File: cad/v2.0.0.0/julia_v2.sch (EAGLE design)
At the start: 32 parts, among them J1 NHD-5.0-800480TF-ATXL-CTP_LCD, J2 NHD-5.0-800480TF-ATXL-CTP_TOU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, U1 RMLV0416EGSB-4S2HA1, U2 EP2C5T144I8, U3 FAN5333BSX, U4 NCP565ST12T3G, U5 LP3965EMP-3.3/NOPB, U6 LP3965EMP-3.3/NOPB

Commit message: v2 update, power and config chip
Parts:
- added C14: 0.1uF, microbuilder:CAP_CERAMIC0805
- added C15: 4.7uF, ik:CPOL
- added FB1: 600R/1A, microbuilder:FERRITE
- added J3: ISP Header (AS), fab:CONN_05X2SHD
- added J4: JTAG Header, fab:CONN_05X2SHD
- added LED1, LED3: RED, led:LEDCHIPLED_0805
- added LED2: GREEN, led:LEDCHIPLED_0805
- added OSC1: (no value), ik:ASV-50.000MHZ-EJ-T
- added R10, R11, R12, R13, R8, R9: 10k, microbuilder:RESISTOR0805
- added R14, R15, R16: 1k, microbuilder:RESISTOR0805
- added R2, R3, R5: 47, microbuilder:RESISTOR0805
- added R4, R6, R7: 27, microbuilder:RESISTOR0805
- added SJ1: (no value), jumper:SJ2WW
- added TP6: TPB1,27, testpad:TPB1,27
- added U$31: EPCQ4ASI8N, ik:EPCQ4ASI8N
- R1: device microbuilder:RESISTOR_0805MP -> microbuilder:RESISTOR0805
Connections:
- new net ADSO: U$31.DATA0
- new net ASDO: J3.9, U2B.IO_3
- new net CE_N: J3.6, R9.2, U2A.!CE
- new net CONFIG_N: J3.5, R10.1, U2A.!CONFIG
- new net CONF_DONE: J3.3, LED2.C, R12.1, U2A.CONF_DONE
- new net CSO_N: J3.8, U$31.CS_N, U2B.IO_2
- new net DATA0: J3.7, R8.1, U$31.DATA1, U2A.DATA0
- new net DCLK: J3.1, R6.1, U$31.DCLK
- new net GCLK: R4.1, TP6.TP, U2A.CLK7
- new net JTAG_TCK: J4.1, R7.2
- new net JTAG_TDI: J4.9, R16.1, U2B.TDI
- new net JTAG_TDO: J4.3, U2B.TDO
- new net JTAG_TMS: J4.5, R15.1, U2B.TMS
- new net N$10: R14.2, R7.1, U2B.TCK
- new net N$11: C2.P$1, L1.2, SJ1.2, U3.VIN
- new net N$2: LED1.A, R2.2
- new net N$3: C14.P$1, C15.+, FB1.P$2, OSC1.EN, OSC1.VDD
- new net N$5: OSC1.OUT, R4.2
- new net N$6: LED3.A, R5.2
- new net N$7: R13.1, R6.2, U2A.DCLK
- new net N$9: LED2.A, R3.2
- new net STATUS_N: R11.1, U2A.!STATUS
- net 3V3IO: now also FB1.P$1, J3.4, J4.4, LED3.C, R10.2, R11.2, R12.2, R13.2, R15.2, R16.2, R8.2, U$31.VCC@1, U$31.VCC@2, U$31.VCC@3
- net GND: now also C14.P$2, C15.-, J3.10, J3.2, J4.10, J4.2, OSC1.GND, R14.1, R2.1, R3.1, R5.1, R9.1, U$31.GND, U2A.CLK0, U2A.CLK1, U2A.CLK2, U2A.CLK3, U2A.CLK4, U2A.CLK5, U2A.CLK6, U2B.MSEL0, U2B.MSEL1
- net VCC3V3: now also LED1.C, SJ1.3; no longer C2.P$1, L1.2, U3.VIN
- net VIN: now also F1.2, SJ1.1
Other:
- note added: "MSEL0/1 0,0 for AS (20MHz)"
- moved on the sheet: U2A, U2B, U2C

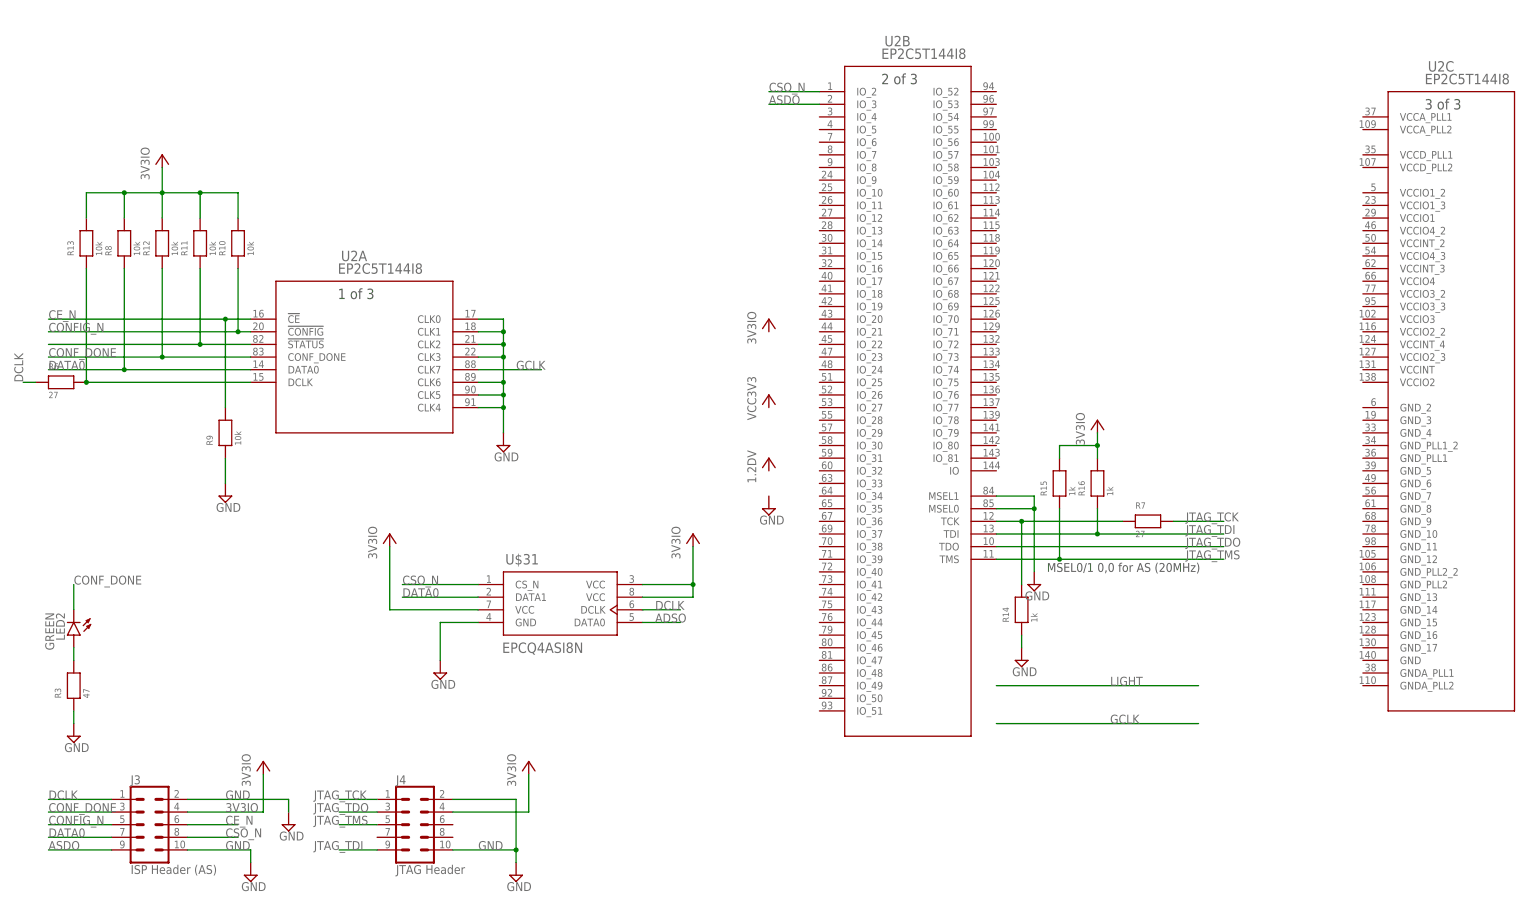
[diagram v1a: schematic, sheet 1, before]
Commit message: Julia v2.0.0.0 schematic and BOM
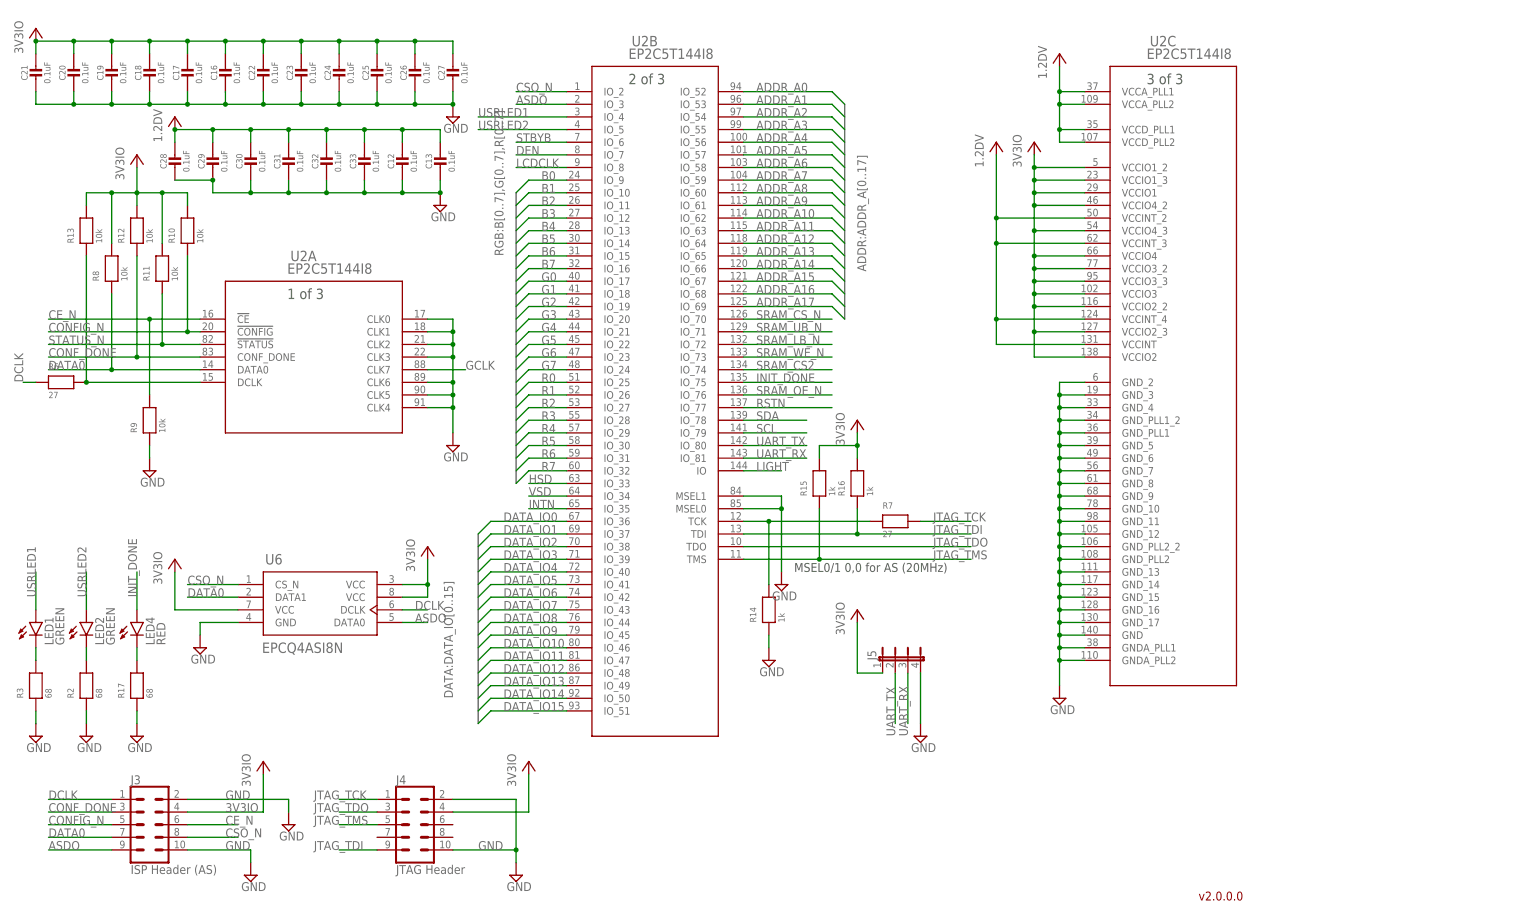
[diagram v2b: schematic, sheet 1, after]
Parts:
- removed TP3: TPB1,27, testpad:TPB1,27
- removed U$31: EPCQ4ASI8N, ik:EPCQ4ASI8N
- added C16, C17, C18, C19, C20, C21, C22, C23, C24, C25, C26, C27, C28, C29, C30, C31, C32, C33: 0.1uF, microbuilder:CAP_CERAMIC0805
- added J5: (no value), jumper:JP4E
- added LED4: RED, led:LEDCHIPLED_0805
- added R17: 68, microbuilder:RESISTOR0805
- added TP7: TPB1,27, testpad:TPB1,27
- C12: value 68uF -> 0.1uF; device microbuilder:CAP_CERAMIC1206 -> microbuilder:CAP_CERAMIC0805; DPN 445-14673-1-ND -> 478-12799-1-ND; MPN C3216X5R1A686M160AC -> 0805ZD104KAT2A
- C13: value 33uF -> 0.1uF; device ik:CPOL -> microbuilder:CAP_CERAMIC0805; DPN 478-5350-1-ND -> 478-12799-1-ND; MPN TLJP336M010R3500 -> 0805ZD104KAT2A
- F1: value (none) -> 3.5A
- LED1: value RED -> GREEN; DPN 67-1552-1-ND -> 67-1553-1-ND; MPN SML-LXT0805IW-TR -> ML-LXT0805IW-TR
- OSC1: value (none) -> 50MHz
- R10, R11, R12, R13, R8, R9: DPN (none) -> 311-10.0KCRCT-ND; MPN (none) -> RC0805FR-0710KL
- R14, R15, R16: DPN (none) -> 311-1.00KCRCT-ND; MPN (none) -> RC0805FR-071KL
- R2, R3: value 47 -> 68; DPN (none) -> 311-68.0CRCT-ND; MPN (none) -> RC0805FR-0768RL
- R4: value 27 -> 68; DPN (none) -> 311-68.0CRCT-ND; MPN (none) -> RC0805FR-0768RL
- R5: value 47 -> 27; DPN (none) -> 311-27ARCT-ND; MPN (none) -> RC0805JR-0727RL
- R6, R7: DPN (none) -> 311-27ARCT-ND; MPN (none) -> RC0805JR-0727RL
- U2: DPN (none) -> 544-2138-ND; MPN (none) -> EP2C5T144I8
- U6: value LP3965EMP-3.3/NOPB -> EPCQ4ASI8N; device ik:LP3965EMP-3.3/NOPB -> ik:EPCQ4ASI8N
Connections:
- removed net ADSO: U$31.DATA0
- removed net CLKIN: J1.CLKIN
- removed net N$2: LED1.A, R2.2
- removed net N$4: C5.P$1
- removed net VCC3V3: C13.+, LED1.C, SJ1.3, TP3.TP, U6.SENSE, U6.VOUT
- new net INIT_DONE: LED4.A, U2B.IO_75
- new net LCDCLK: J1.CLKIN, U2B.IO_8
- new net N$12: LED4.C, R17.2
- new net N$13: LED2.C, R2.2
- new net UART_RX: J5.3, U2B.IO_81
- new net UART_TX: J5.2, U2B.IO_80
- new net USRLED1: LED1.A, U2B.IO_4
- new net USRLED2: LED2.A, U2B.IO_5
- net 1.2DV: now also C12.P$1, C13.P$1, C28.P$1, C29.P$1, C30.P$1, C31.P$1, C32.P$1, C33.P$1, U2C.VCCA_PLL1, U2C.VCCA_PLL2, U2C.VCCD_PLL1, U2C.VCCD_PLL2, U2C.VCCINT, U2C.VCCINT_2, U2C.VCCINT_3, U2C.VCCINT_4
- net 3V3IO: now also C16.P$1, C17.P$1, C18.P$1, C19.P$1, C20.P$1, C21.P$1, C22.P$1, C23.P$1, C24.P$1, C25.P$1, C26.P$1, C27.P$1, C5.P$1, J5.1, LED3.A, SJ1.3, U2C.VCCIO1, U2C.VCCIO1_2, U2C.VCCIO1_3, U2C.VCCIO2, U2C.VCCIO2_2, U2C.VCCIO2_3, U2C.VCCIO3, U2C.VCCIO3_2, U2C.VCCIO3_3, U2C.VCCIO4, U2C.VCCIO4_2, U2C.VCCIO4_3, U6.VCC@1, U6.VCC@2, U6.VCC@3; no longer LED3.C, U$31.VCC@1, U$31.VCC@2, U$31.VCC@3
- net ADDR_A0: now also U2B.IO_52
- net ADDR_A1: now also U2B.IO_53
- net ADDR_A10: now also U2B.IO_62
- net ADDR_A11: now also U2B.IO_63
- net ADDR_A12: now also U2B.IO_64
- net ADDR_A13: now also U2B.IO_65
- net ADDR_A14: now also U2B.IO_66
- net ADDR_A15: now also U2B.IO_67
- net ADDR_A16: now also U2B.IO_68
- net ADDR_A17: now also U2B.IO_69
- net ADDR_A2: now also U2B.IO_54
- net ADDR_A3: now also U2B.IO_55
- net ADDR_A4: now also U2B.IO_56
- net ADDR_A5: now also U2B.IO_57
- net ADDR_A6: now also U2B.IO_58
- net ADDR_A7: now also U2B.IO_59
- net ADDR_A8: now also U2B.IO_60
- net ADDR_A9: now also U2B.IO_61
- net ASDO: now also U6.DATA0
- net B0: now also U2B.IO_9
- net B1: now also U2B.IO_10
- net B2: now also U2B.IO_11
- net B3: now also U2B.IO_12
- net B4: now also U2B.IO_13
- net B5: now also U2B.IO_14
- net B6: now also U2B.IO_15
- net B7: now also U2B.IO_16
- net CONF_DONE: no longer LED2.C
- net CSO_N: now also U6.CS_N; no longer U$31.CS_N
- net DATA0: now also U6.DATA1; no longer U$31.DATA1
- net DATA_IO0: now also U2B.IO_36
- net DATA_IO1: now also U2B.IO_37
- net DATA_IO10: now also U2B.IO_46
- net DATA_IO11: now also U2B.IO_47
- net DATA_IO12: now also U2B.IO_48
- net DATA_IO13: now also U2B.IO_49
- net DATA_IO14: now also U2B.IO_50
- net DATA_IO15: now also U2B.IO_51
- net DATA_IO2: now also U2B.IO_38
- net DATA_IO3: now also U2B.IO_39
- net DATA_IO4: now also U2B.IO_40
- net DATA_IO5: now also U2B.IO_41
- net DATA_IO6: now also U2B.IO_42
- net DATA_IO7: now also U2B.IO_43
- net DATA_IO8: now also U2B.IO_44
- net DATA_IO9: now also U2B.IO_45
- net DCLK: now also U6.DCLK; no longer U$31.DCLK
- net DEN: now also U2B.IO_7
- net G0: now also U2B.IO_17
- net G1: now also U2B.IO_18
- net G2: now also U2B.IO_19
- net G3: now also U2B.IO_20
- net G4: now also U2B.IO_21
- net G5: now also U2B.IO_22
- net G6: now also U2B.IO_23
- net G7: now also U2B.IO_24
- net GCLK: now also R5.1; no longer R4.1
- net GND: now also C13.P$2, C16.P$2, C17.P$2, C18.P$2, C19.P$2, C20.P$2, C21.P$2, C22.P$2, C23.P$2, C24.P$2, C25.P$2, C26.P$2, C27.P$2, C28.P$2, C29.P$2, C30.P$2, C31.P$2, C32.P$2, C33.P$2, J5.4, R17.1, R4.1, U2C.GND, U2C.GNDA_PLL1, U2C.GNDA_PLL2, U2C.GND_10, U2C.GND_11, U2C.GND_12, U2C.GND_13, U2C.GND_14, U2C.GND_15, U2C.GND_16, U2C.GND_17, U2C.GND_2, U2C.GND_3, U2C.GND_4, U2C.GND_5, U2C.GND_6, U2C.GND_7, U2C.GND_8, U2C.GND_9, U2C.GND_PLL1, U2C.GND_PLL1_2, U2C.GND_PLL2, U2C.GND_PLL2_2, U6.GND; no longer C13.-, R5.1, U$31.GND, U6.GND/TAB
- net HSD: now also U2B.IO_33
- net INTN: now also U2B.IO_35
- net LIGHT: now also U2B.IO
- net N$5: now also R5.2; no longer R4.2
- net N$6: now also LED3.C, R4.2; no longer LED3.A, R5.2
- net N$9: now also LED1.C; no longer LED2.A
- net R0: now also U2B.IO_25
- net R1: now also U2B.IO_26
- net R2: now also U2B.IO_27
- net R3: now also U2B.IO_28
- net R4: now also U2B.IO_29
- net R5: now also U2B.IO_30
- net R6: now also U2B.IO_31
- net R7: now also U2B.IO_32
- net RSTN: now also U2B.IO_77
- net SCL: now also U2B.IO_79
- net SDA: now also U2B.IO_78
- net SRAM_CS2: now also U2B.IO_74
- net SRAM_CS_N: now also U2B.IO_70
- net SRAM_LB_N: now also U2B.IO_72
- net SRAM_OE_N: now also U2B.IO_76
- net SRAM_UB_N: now also U2B.IO_71
- net SRAM_WE_N: now also U2B.IO_73
- net STATUS_N: now also TP7.TP
- net STBYB: now also U2B.IO_6
- net VIN: no longer C12.P$1, U6.SD_N, U6.VIN
- net VSD: now also U2B.IO_34
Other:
- note added: "v2.0.0.0"
- moved on the sheet: CN1, F1, LED2, LED3, R10, R11, R12, R13, R14, R15, R16, R3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

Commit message: Julia v2.0.0.0 board
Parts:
- removed C25, C26, C27, C28, C29, C30, C31, C32, C33: 0.1uF, microbuilder:CAP_CERAMIC0805
- removed TP1, TP6, TP7: TPB1,27, testpad:TPB1,27
- added TP3: TPB1,27, testpad:TPB1,27
- U1: value RMLV0416EGSB-4S2HA1 -> RMLV0816BGSB-4S2#AA0; device ultralibrarian:RMLV0416EGSB-4S2HA1 -> ik:RMLV0816BGSB-4S2#AA0; DPN RMLV0416EGSB-4S2 -> (none); MPN RMLV0416EGSB-4S2#HA1 -> (none)
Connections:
- net N$11 renamed F_VIN
- net N$3 renamed OSC_V
- net N$5 renamed _GCLK
- net N$8 renamed F_SW
- removed net SRAM_CS2: U1A.CS2, U2B.IO_74
- new net ADDR_A18: U1A.A18, U2B.IO_70
- net 1.2DV: now also C22.P$1, C23.P$1, TP3.TP; no longer C28.P$1, C29.P$1, C30.P$1, C31.P$1, C32.P$1, C33.P$1, TP4.TP
- net 3V3IO: no longer C22.P$1, C23.P$1, C25.P$1, C26.P$1, C27.P$1
- net ADDR_A0: now also U2B.IO_36; no longer U2B.IO_52
- net ADDR_A1: now also U2B.IO_37; no longer U2B.IO_53
- net ADDR_A2: now also U2B.IO_38; no longer U2B.IO_54
- net ADDR_A3: now also U2B.IO_39; no longer U2B.IO_55
- net ADDR_A4: now also U2B.IO_40; no longer U2B.IO_56
- net ADDR_A5: now also U2B.IO_45; no longer U2B.IO_57
- net ADDR_A6: now also U2B.IO_51; no longer U2B.IO_58
- net ADDR_A7: now also U2B.IO_52; no longer U2B.IO_59
- net B0: now also U2B.IO_16; no longer U2B.IO_9
- net B1: now also U2B.IO_15; no longer U2B.IO_10
- net B2: now also U2B.IO_14; no longer U2B.IO_11
- net B3: now also U2B.IO_13; no longer U2B.IO_12
- net B4: now also U2B.IO_12; no longer U2B.IO_13
- net B5: now also U2B.IO_11; no longer U2B.IO_14
- net B6: now also U2B.IO_10; no longer U2B.IO_15
- net B7: now also U2B.IO_9; no longer U2B.IO_16
- net DATA_IO0: now also U2B.IO_47; no longer U2B.IO_36
- net DATA_IO1: now also U2B.IO_48; no longer U2B.IO_37
- net DATA_IO10: now also U2B.IO_57; no longer U2B.IO_46
- net DATA_IO11: now also U2B.IO_56; no longer U2B.IO_47
- net DATA_IO12: now also U2B.IO_55; no longer U2B.IO_48
- net DATA_IO13: now also U2B.IO_54; no longer U2B.IO_49
- net DATA_IO14: now also U2B.IO_53; no longer U2B.IO_50
- net DATA_IO15: now also U2B.IO_74; no longer U2B.IO_51
- net DATA_IO2: now also U2B.IO_49; no longer U2B.IO_38
- net DATA_IO3: now also U2B.IO_50; no longer U2B.IO_39
- net DATA_IO4: now also U2B.IO_41; no longer U2B.IO_40
- net DATA_IO5: now also U2B.IO_42; no longer U2B.IO_41
- net DATA_IO6: now also U2B.IO_43; no longer U2B.IO_42
- net DATA_IO7: now also U2B.IO_44; no longer U2B.IO_43
- net DATA_IO8: now also U2B.IO_59; no longer U2B.IO_44
- net DATA_IO9: now also U2B.IO_58; no longer U2B.IO_45
- net G0: now also U2B.IO_24; no longer U2B.IO_17
- net G1: now also U2B.IO_23; no longer U2B.IO_18
- net G2: now also U2B.IO_22; no longer U2B.IO_19
- net G3: now also U2B.IO_21; no longer U2B.IO_20
- net G4: now also U2B.IO_20; no longer U2B.IO_21
- net G5: now also U2B.IO_19; no longer U2B.IO_22
- net G6: now also U2B.IO_18; no longer U2B.IO_23
- net G7: now also U2B.IO_17; no longer U2B.IO_24
- net GCLK: now also TP4.TP; no longer TP6.TP
- net GND: no longer C25.P$2, C26.P$2, C27.P$2, C28.P$2, C29.P$2, C30.P$2, C31.P$2, C32.P$2, C33.P$2, TP5.TP
- net R0: now also U2B.IO_32; no longer U2B.IO_25
- net R1: now also U2B.IO_31; no longer U2B.IO_26
- net R2: now also U2B.IO_30; no longer U2B.IO_27
- net R3: now also U2B.IO_29; no longer U2B.IO_28
- net R4: now also U2B.IO_28; no longer U2B.IO_29
- net R5: now also U2B.IO_27; no longer U2B.IO_30
- net R6: now also U2B.IO_26; no longer U2B.IO_31
- net R7: now also U2B.IO_25; no longer U2B.IO_32
- net SRAM_CS_N: now also U2B.IO_46; no longer U2B.IO_70
- net SRAM_LB_N: now also U2B.IO_71; no longer U2B.IO_72
- net SRAM_UB_N: now also U2B.IO_72; no longer U2B.IO_71
- net STATUS_N: now also TP5.TP; no longer TP7.TP
- net VIN: no longer TP1.TP
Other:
- moved on the sheet: C12, C13, C16, C17, C18, C19, C20, C21, C22, C23, C24, TP4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
